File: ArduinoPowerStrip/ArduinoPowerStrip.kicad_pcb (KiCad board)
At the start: 2 copper layers, 53.3 x 68.5 mm, 15 parts, among them P101 Triac1, P102 Triac1, Q101 Q_NPN_BEC, Q102 Q_NPN_BEC, U101 MOC3041M, U102 MOC3041M, U103 TRIAC, U104 TRIAC

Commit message: Initial draft of the final board
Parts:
- removed ArduinoPowerStrip: ARDUINO_SHIELD, ArduinoShield:ArduinoShield
- added R107: 361, Resistors_ThroughHole:Resistor_Horizontal_RM10mm, F.Cu at (76.5, 101.5)
- added R108: 331, Resistors_ThroughHole:Resistor_Horizontal_RM10mm, F.Cu at (80.0, 102.5)
- added SHIELD101: ARDUINO_SHIELD, ArduinoShield:ArduinoShield, F.Cu at (123.3, 116.2)
- P101: value Triac1 -> Con1
- P102: value Triac1 -> Con2
- Q101, Q102: value Q_NPN_BEC -> BC847-SOT23; footprint TO_SOT_Packages_SMD:SOT-23 -> TO_SOT_Packages_SMD:SOT-23_Handsoldering; moved to F.Cu
- R101, R102: value R_Small -> 331; moved to F.Cu
- R103: value R_Small -> 131; moved to F.Cu
- R104: value R_Small -> 361; footprint Resistors_SMD:R_1206 -> Resistors_ThroughHole:Resistor_Horizontal_RM10mm; moved to F.Cu
- R105: value R_Small -> 331
- R106: value R_Small -> 131; footprint Resistors_ThroughHole:Resistor_Horizontal_RM10mm -> Resistors_SMD:R_1206
- U102: value MOC3041M -> BTA06-600BW; footprint Housings_DIP:DIP-6_W7.62mm_LongPads -> TO_SOT_Packages_THT:TO-220_Neutral123_Horizontal_LargePads; moved to B.Cu
- U103: value TRIAC -> MOC3041M; footprint TO_SOT_Packages_THT:TO-220_Neutral123_Horizontal_Reverse_LargePads -> Housings_DIP:DIP-6_W7.62mm_LongPads; moved to F.Cu
- U104: value TRIAC -> BTA06-600BW; footprint TO_SOT_Packages_THT:TO-220_Neutral123_Horizontal_Reverse_LargePads -> TO_SOT_Packages_THT:TO-220_Neutral123_Horizontal_LargePads
- moved U104 65.5 mm to (85.0, 95.0)
- moved P102 62.8 mm to (85.0, 109.0), turned to 0 degrees
- moved R106 52.4 mm to (95.0, 61.0), turned to 0 degrees
- moved U103 50.9 mm to (87.6, 63.5), turned to 270 degrees
- moved Q102 48.9 mm to (90.0, 57.0), turned to 270 degrees
- moved U102 48.4 mm to (108.0, 95.0), turned to 180 degrees
- moved R104 46.5 mm to (120.0, 97.5)
- moved R102 39.2 mm to (80.0, 56.0)
- moved R101 39.1 mm to (80.0, 52.5)
- moved R105 33.1 mm to (103.0, 102.5), turned to 0 degrees
- moved R103 30.4 mm to (101.0, 61.0), turned to 180 degrees
- moved Q101 25.4 mm to (100.0, 53.5), turned to 270 degrees
- moved U101 19.5 mm to (112.0, 63.5)
- moved P101 18.0 mm to (108.0, 109.0), turned to 0 degrees
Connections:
- R104 pad 1: Net-(R104-Pad1) -> /Triac1L
- R104 pad 2: /Gnd -> Net-(R104-Pad2)
- R105 pad 1: /Triac1L -> Net-(R105-Pad1)
- R105 pad 2: Net-(R105-Pad2) -> /Triac1O
- R106 pad 1: /Triac2L -> Net-(R106-Pad1)
- R106 pad 2: Net-(R106-Pad2) -> /Gnd
- U101 pad 4: Net-(U101-Pad4) -> Net-(R105-Pad1)
- U101 pad 6: Net-(R105-Pad2) -> Net-(R104-Pad2)
- U102 pad 1: Net-(R104-Pad1) -> /Triac1O
- U102 pad 2: /Q2Out -> /Triac1L
- U102 pad 3: (no net) -> Net-(R105-Pad1)
- U103 pad 1: /Triac1O -> Net-(R106-Pad1)
- U103 pad 2: /Triac1L -> /Q2Out
- U103 pad 3: Net-(U101-Pad4) -> (no net)
- U104 pad 3: Net-(U102-Pad4) -> Net-(R108-Pad1)
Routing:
- net Net-(U102-Pad4): track 38.3 -> 0.00 mm
- net Net-(U101-Pad4): track 37.9 -> 0.00 mm
- net Net-(R107-Pad2): track 0.00 -> 34.6 mm
- net Net-(R105-Pad1): track 0.00 -> 34.0 mm
- net Net-(Q102-Pad1): track 29.0 -> 7.07 mm
- net Net-(R104-Pad2): track 0.00 -> 19.5 mm
- net Net-(Q101-Pad1): track 4.17 -> 17.8 mm
- net /Q1Out: track 7.85 -> 17.2 mm, vias 0 -> 1
- net Net-(R106-Pad2): track 8.91 -> 0.00 mm
- net Net-(R108-Pad1): track 0.00 -> 8.52 mm
- net Net-(R106-Pad1): track 0.00 -> 7.74 mm
- net Net-(R103-Pad1): track 5.07 -> 11.3 mm
- net Net-(R104-Pad1): track 4.95 -> 0.00 mm
- net /Triac1O: track 11.4 -> 16.1 mm
- net /Triac2L: track 29.6 -> 25.0 mm
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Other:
- outline, holes or cut-outs redrawn
- rule pad_to_mask_clearance: 0.2 -> 0

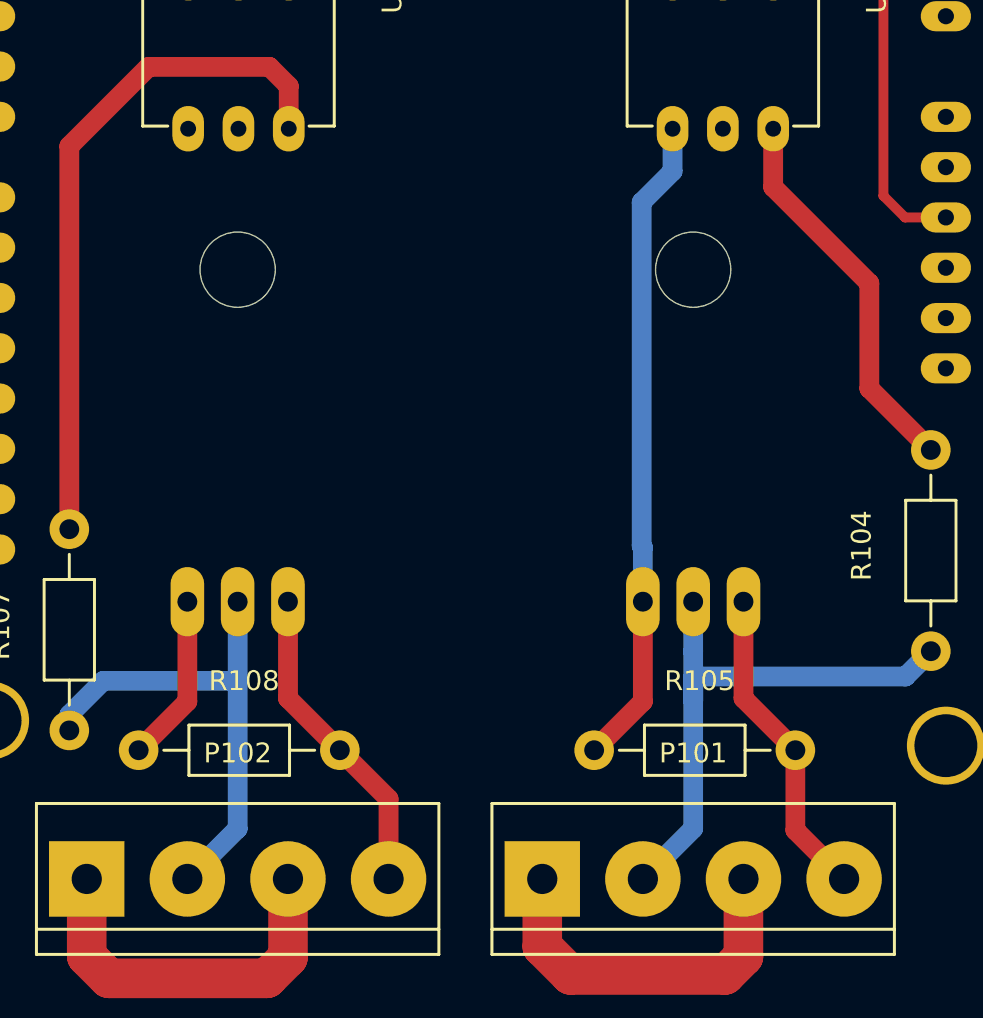
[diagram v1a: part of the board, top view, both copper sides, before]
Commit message: Double sided board and separeted Power signals
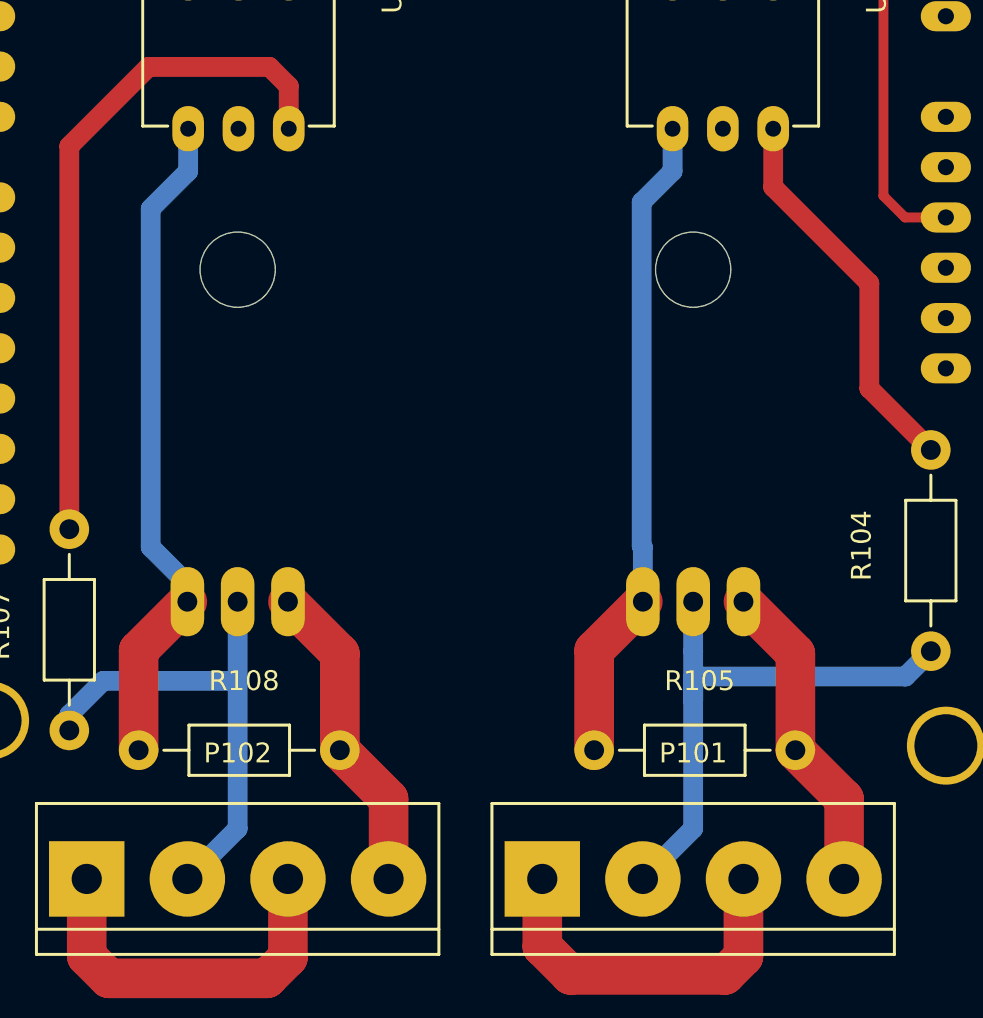
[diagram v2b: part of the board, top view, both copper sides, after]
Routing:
- net Net-(R108-Pad1): track 8.52 -> 33.9 mm
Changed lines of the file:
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@@
   (general
     (links 28)
-    (no_connects 0)
-    (area 64.426 47.269499 124.785 120.98297)
+    (no_connects 1)
+    (area 52.000001 38.9 124.785 120.98297)
     (thickness 1.6)
-    (drawings 9)
-    (tracks 93)
+    (drawings 11)
+    (tracks 98)
     (zones 0)
     (modules 17)
@@
   )
   (setup
-    (last_trace_width 0.5)
+    (last_trace_width 1)
     (user_trace_width 0.5)
     (user_trace_width 1)
@@
     (mod_text_size 1 1)
     (mod_text_width 0.15)
-    (pad_size 1.5 1.5)
-    (pad_drill 0.6)
+    (pad_size 3.937 3.937)
+    (pad_drill 3.175)
     (pad_to_mask_clearance 0)
     (aux_axis_origin 0 0)
+    (grid_origin 70 116.25)
     (visible_elements FFFCFF7F)
     (pcbplotparams
-      (layerselection 0x00030_80000001)
+      (layerselection 0x010fc_80000001)
       (usegerberextensions false)
       (excludeedgelayer true)
@@
       (psa4output false)
       (plotreference true)
-      (plotvalue true)
+      (plotvalue false)
       (plotinvisibletext false)
       (padsonsilk false)
@@
       (outputformat 1)
       (mirror false)
-      (drillshape 1)
+      (drillshape 0)
       (scaleselection 1)
-      (outputdirectory ""))
+      (outputdirectory ../../../../Desktop/Gerbers/))
   )
   (net 0 "")
@@
     (pad 5V thru_hole oval (at 38.1 -2.54 180) (size 2.54 1.524) (drill 0.8128) (layers *.Cu *.Mask F.SilkS)
       (net 44 "Net-(SHIELD101-Pad5V)"))
-    (pad "" thru_hole circle (at 66.04 -7.62 180) (size 3.937 3.937) (drill 3.175) (layers *.Cu *.Mask F.SilkS))
-    (pad "" thru_hole circle (at 66.04 -35.56 180) (size 3.937 3.937) (drill 3.175) (layers *.Cu *.Mask F.SilkS))
-    (pad "" thru_hole circle (at 15.24 -50.8 180) (size 3.937 3.937) (drill 3.175) (layers *.Cu *.Mask F.SilkS))
-    (pad "" thru_hole circle (at 13.97 -2.54 180) (size 3.937 3.937) (drill 3.175) (layers *.Cu *.Mask F.SilkS))
+    (pad "" np_thru_hole circle (at 66.04 -7.62 180) (size 3.937 3.937) (drill 3.175) (layers *.Cu *.Mask F.SilkS))
+    (pad "" np_thru_hole circle (at 66.04 -35.56 180) (size 3.937 3.937) (drill 3.175) (layers *.Cu *.Mask F.SilkS))
+    (pad "" np_thru_hole circle (at 15.24 -50.8 180) (size 3.937 3.937) (drill 3.175) (layers *.Cu *.Mask F.SilkS))
+    (pad "" np_thru_hole circle (at 13.97 -2.54 180) (size 3.937 3.937) (drill 3.175) (layers *.Cu *.Mask F.SilkS))
   )
   (module Housings_DIP:DIP-6_W7.62mm_LongPads (layer F.Cu)
@@
     )
   )
+  (dimension 53.5 (width 0.3) (layer Eco2.User)
+    (gr_text "53.500 mm" (at 96.75 40.4) (layer Eco2.User)
+      (effects (font (size 1.5 1.5) (thickness 0.3)))
+    )
+    (feature1 (pts (xy 123.5 47.75) (xy 123.5 39.05)))
+    (feature2 (pts (xy 70 47.75) (xy 70 39.05)))
+    (crossbar (pts (xy 70 41.75) (xy 123.5 41.75)))
+    (arrow1a (pts (xy 123.5 41.75) (xy 122.373496 42.336421)))
+    (arrow1b (pts (xy 123.5 41.75) (xy 122.373496 41.163579)))
+    (arrow2a (pts (xy 70 41.75) (xy 71.126504 42.336421)))
+    (arrow2b (pts (xy 70 41.75) (xy 71.126504 41.163579)))
+  )
+  (dimension 68.5 (width 0.3) (layer Eco2.User)
+    (gr_text "68.500 mm" (at 58.65 82 90) (layer Eco2.User)
+      (effects (font (size 1.5 1.5) (thickness 0.3)))
+    )
+    (feature1 (pts (xy 70 47.75) (xy 57.3 47.75)))
+    (feature2 (pts (xy 70 116.25) (xy 57.3 116.25)))
+    (crossbar (pts (xy 60 116.25) (xy 60 47.75)))
+    (arrow1a (pts (xy 60 47.75) (xy 60.586421 48.876504)))
+    (arrow1b (pts (xy 60 47.75) (xy 59.413579 48.876504)))
+    (arrow2a (pts (xy 60 116.25) (xy 60.586421 115.123496)))
+    (arrow2b (pts (xy 60 116.25) (xy 59.413579 115.123496)))
+  )
   (gr_line (start 70 51.5) (end 70 116.2) (layer Edge.Cuts) (width 0.1))
   (gr_line (start 71.3 50.2) (end 70 51.5) (layer Edge.Cuts) (width 0.1))
@@
   (segment (start 101.811495 113.846942) (end 100.38 112.415447) (width 2) (layer F.Cu) (net 2))
   (segment (start 100.38 112.415447) (end 100.38 109) (width 2) (layer F.Cu) (net 2))
-  (segment (start 113.16 102.5) (end 113.16 106.54) (width 1) (layer F.Cu) (net 3))
-  (segment (start 113.16 106.54) (end 115.62 109) (width 1) (layer F.Cu) (net 3))
-  (segment (start 110.54 95) (end 110.54 99.88) (width 1) (layer F.Cu) (net 3))
-  (segment (start 110.54 99.88) (end 113.16 102.5) (width 1) (layer F.Cu) (net 3))
+  (segment (start 113.16 102.5) (end 113.16 97.62) (width 2) (layer F.Cu) (net 3))
+  (segment (start 113.16 97.62) (end 110.54 95) (width 2) (layer F.Cu) (net 3))
+  (segment (start 115.62 109) (end 115.62 104.96) (width 2) (layer F.Cu) (net 3))
+  (segment (start 115.62 104.96) (end 113.16 102.5) (width 2) (layer F.Cu) (net 3))
   (segment (start 76.5 101.5) (end 76.5 100.713307) (width 1) (layer B.Cu) (net 4))
   (segment (start 76.5 100.713307) (end 78.213307 99) (width 1) (layer B.Cu) (net 4))
@@
   (segment (start 86.48175 114.01825) (end 87.54 112.96) (width 2) (layer F.Cu) (net 5))
   (segment (start 87.54 112.96) (end 87.54 109) (width 2) (layer F.Cu) (net 5))
-  (segment (start 92.62 109) (end 92.62 104.96) (width 1) (layer F.Cu) (net 6))
-  (segment (start 92.62 104.96) (end 90.16 102.5) (width 1) (layer F.Cu) (net 6))
-  (segment (start 87.54 95) (end 87.54 99.88) (width 1) (layer F.Cu) (net 6))
-  (segment (start 87.54 99.88) (end 90.16 102.5) (width 1) (layer F.Cu) (net 6))
+  (segment (start 90.16 102.5) (end 90.16 97.62) (width 2) (layer F.Cu) (net 6))
+  (segment (start 90.16 97.62) (end 87.54 95) (width 2) (layer F.Cu) (net 6))
+  (segment (start 92.62 109) (end 92.62 104.96) (width 2) (layer F.Cu) (net 6))
+  (segment (start 92.62 104.96) (end 90.16 102.5) (width 2) (layer F.Cu) (net 6))
   (segment (start 81.45 52.5) (end 83.859876 52.5) (width 0.5) (layer F.Cu) (net 7))
   (segment (start 83.859876 52.5) (end 84.808786 53.44891) (width 0.5) (layer F.Cu) (net 7))
@@
   (segment (start 116.894517 78.922787) (end 116.894517 84.234517) (width 1) (layer F.Cu) (net 15))
   (segment (start 116.894517 84.234517) (end 120 87.34) (width 1) (layer F.Cu) (net 15))
+  (segment (start 103 102.5) (end 103 97.46) (width 2) (layer F.Cu) (net 16))
+  (segment (start 103 97.46) (end 105.46 95) (width 2) (layer F.Cu) (net 16))
   (segment (start 105.46 95) (end 105.46 92.24994) (width 1) (layer B.Cu) (net 16))
   (segment (start 105.46 92.24994) (end 105.400079 92.190019) (width 1) (layer B.Cu) (net 16))
@@
   (segment (start 105.400079 74.829921) (end 106.96 73.27) (width 1) (layer B.Cu) (net 16))
   (segment (start 106.96 73.27) (end 106.96 71.12) (width 1) (layer B.Cu) (net 16))
-  (segment (start 105.46 95) (end 105.46 100.04) (width 1) (layer F.Cu) (net 16))
-  (segment (start 105.46 100.04) (end 103 102.5) (width 1) (layer F.Cu) (net 16))
   (segment (start 105.46 94.09957) (end 105.46 95) (width 1) (layer F.Cu) (net 16))
   (segment (start 93.55 61) (end 88.829585 61) (width 0.5) (layer F.Cu) (net 17))
@@
   (segment (start 86.61 68) (end 87.58 68.97) (width 1) (layer F.Cu) (net 18))
   (segment (start 87.58 68.97) (end 87.58 71.12) (width 1) (layer F.Cu) (net 18))
-  (segment (start 82.46 95) (end 82.46 100.04) (width 1) (layer F.Cu) (net 19))
-  (segment (start 82.46 100.04) (end 80 102.5) (width 1) (layer F.Cu) (net 19))
+  (segment (start 82.46 94.09957) (end 82.46 95) (width 1) (layer B.Cu) (net 19))
+  (segment (start 82.5 71.12) (end 82.5 73.27) (width 1) (layer B.Cu) (net 19))
+  (segment (start 80.61037 92.24994) (end 82.46 94.09957) (width 1) (layer B.Cu) (net 19))
+  (segment (start 82.5 73.27) (end 80.61037 75.15963) (width 1) (layer B.Cu) (net 19))
+  (segment (start 80.61037 75.15963) (end 80.61037 92.24994) (width 1) (layer B.Cu) (net 19))
+  (segment (start 80 102.5) (end 80 97.46) (width 2) (layer F.Cu) (net 19))
+  (segment (start 80 97.46) (end 82.46 95) (width 2) (layer F.Cu) (net 19))
 )
